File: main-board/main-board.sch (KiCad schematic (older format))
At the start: 69 parts, among them J1 NVIDIA_Jetson_NX_Dev_40pin_Co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, J10 FSESC_6.6_COMM_Minimal, J11 FSESC_6.6_COMM_Minimal, J12 FSESC_6.6_COMM_Minimal, J13 FSESC_6.6_COMM_Minimal, J14 ArducamPTZ, J2 NVIDIA_Jetson_NX_Dev_Button_C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, J3 Conn_01x02, J4 Conn_01x02, J5 Conn_01x02, J6 FSESC_6.6_COMM_Minimal, J7 QWIIC_Generic_Conn, J8 Conn_01x03, J9 FSESC_6.6_COMM_Minimal, M1 Fan_3pin, M2 Fan_3pin, M3 Fan_3pin, Q1 Q_NMOS_GSD, Q2 Q_NMOS_GSD, Q4 Q_NMOS_GSD, Q5 Q_NMOS_GSD, Q6 Q_NMOS_GSD, Q7 Q_NMOS_GSD, Q8 Q_NMOS_GSD, U1 RFM95W_Adafruit_Breakout, U10 Analog Temp Sensor, U11 Adafruit_GPS_V3, U12 SN74AHCT125D, U2 TDK_I3A4W008A033V, U3 TDK_I3A4W008A033V, U5 Teensy_4.1, U6 Analog Temp Sensor, U7 Analog Temp Sensor, U8 Analog Temp Sensor, U9 Analog Temp Sensor

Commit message: Shooouuulld be fully routed
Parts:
- added J15: Angle Sensor, Connector_JST:JST_PH_B6B-PH-K_1x06_P2.00mm_Vertical, symbol Connector_Generic:Conn_01x06
- added SYM1: SYM_Magnet_Small, symbol Graphic:SYM_Magnet_Small
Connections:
- net +3V3: now also J15.1 (Pin_1)
- net ADC3: now also U5.45 (P38); no longer U5.33 (P26)
- net ADC5: now also U5.33 (P26); no longer U5.48 (P41)
- net ADC_12V: now also U5.47 (P40); no longer U5.46 (P39)
- net ADC_5V: now also U5.46 (P39); no longer U5.45 (P38)
- net ADC_BATT: now also U5.48 (P41); no longer U5.47 (P40)
- net GND: now also J15.2 (Pin_2)
- net M1_RX: now also U5.41 (P34); no longer U5.2 (P0)
- net M1_TX: now also U5.42 (P35); no longer U5.3 (P1)
- net M2_RX: now also U5.35 (P28); no longer U5.9 (P7)
- net M2_TX: now also U5.36 (P29); no longer U5.10 (P8)
- net M4_RX: now also U5.9 (P7); no longer U5.25 (P21)
- net M4_TX: now also U5.10 (P8); no longer U5.24 (P20)
- net M5_RX: now also U5.25 (P21); no longer U5.35 (P28)
- net M5_TX: now also U5.24 (P20); no longer U5.36 (P29)
- net M6_RX: now also U5.2 (P0); no longer U5.41 (P34)
- net M6_TX: now also U5.3 (P1); no longer U5.42 (P35)
- net MISO: now also J15.4 (Pin_4)
- net MOSI: now also J15.3 (Pin_3)
- net SCK: now also J15.5 (Pin_5)
- net Angle_CS: now reaches U5.11 (P9)
- net Angle_CS: now also J15.6 (Pin_6)
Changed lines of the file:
@@
 Text Label 7500 5500 0    50   ~ 0
 ADC2
-Text Label 6600 6500 2    50   ~ 0
+Text Label 7500 6600 0    50   ~ 0
 ADC3
 Text Label 6600 6600 2    50   ~ 0
 ADC4
-Text Label 7500 6300 0    50   ~ 0
+Text Label 6600 6500 2    50   ~ 0
 ADC5
 $Comp
@@
 	8300 9950 8100 9950
 Connection ~ 8750 10150
-Text Label 6600 4900 2    50   ~ 0
+Text Label 7500 7000 0    50   ~ 0
 M1_RX
-Text Label 6600 5000 2    50   ~ 0
+Text Label 7500 6900 0    50   ~ 0
 M1_TX
-Text Label 6600 5600 2    50   ~ 0
+Text Label 6600 6700 2    50   ~ 0
 M2_RX
-Text Label 6600 5700 2    50   ~ 0
+Text Label 6600 6800 2    50   ~ 0
 M2_TX
 Text Label 7500 6000 0    50   ~ 0
@@
 Text Label 7500 5900 0    50   ~ 0
 M3_RX
-Text Label 6600 6700 2    50   ~ 0
+Text Label 7500 5300 0    50   ~ 0
 M5_RX
-Text Label 6600 6800 2    50   ~ 0
+Text Label 7500 5400 0    50   ~ 0
 M5_TX
-Text Label 7500 5400 0    50   ~ 0
+Text Label 6600 5700 2    50   ~ 0
 M4_TX
-Text Label 7500 5300 0    50   ~ 0
+Text Label 6600 5600 2    50   ~ 0
 M4_RX
-Text Label 7500 7000 0    50   ~ 0
+Text Label 6600 4900 2    50   ~ 0
 M6_RX
-Text Label 7500 6900 0    50   ~ 0
-M6_TX
 Text Label 6600 5100 2    50   ~ 0
 ARGB_Data
@@
 Text Label 7500 6700 0    50   ~ 0
 Fan3_Control
-Text Label 7500 6600 0    50   ~ 0
+Text Label 7500 6500 0    50   ~ 0
 ADC_5V
-Text Label 7500 6400 0    50   ~ 0
+Text Label 7500 6300 0    50   ~ 0
 ADC_BATT
 Text Label 8050 3250 0    50   ~ 0
@@
 Text Label 6300 3250 0    50   ~ 0
 ADC_12V
-Text Label 7500 6500 0    50   ~ 0
+Text Label 7500 6400 0    50   ~ 0
 ADC_12V
 $Comp
@@
 	1    0    0    -1
 $EndComp
+$Comp
+L Connector_Generic:Conn_01x06 J15
+U 1 1 6134C702
+P 14050 8800
+F 0 "J15" H 14130 8792 50  0000 L CNN
+F 1 "Angle Sensor" H 14130 8701 50  0000 L CNN
+F 2 "Connector_JST:JST_PH_B6B-PH-K_1x06_P2.00mm_Vertical" H 14050 8800 50  0001 C CNN
+F 3 "AS5047D-ATSTCT-ND" H 14050 8800 50  0001 C CNN
+	1    14050 8800
+	1    0    0    -1
+$EndComp
+$Comp
+L Graphic:SYM_Magnet_Small SYM1
+U 1 1 6134F49B
+P 15000 8850
+F 0 "SYM1" H 15000 8990 50  0001 C CNN
+F 1 "SYM_Magnet_Small" H 15000 8725 50  0001 C CNN
+F 2 "" H 15000 8675 50  0001 C CNN
+F 3 "~" H 15030 8650 50  0001 C CNN
+F 4 "469-1025-ND" H 15000 8850 50  0001 C CNN "Digikey Part Num"
+	1    15000 8850
+	1    0    0    -1
+$EndComp
+$Comp
+L power:+3.3V #PWR0103
+U 1 1 61354FD1
+P 13500 8600
+F 0 "#PWR0103" H 13500 8450 50  0001 C CNN
+F 1 "+3.3V" H 13515 8773 50  0000 C CNN
+F 2 "" H 13500 8600 50  0001 C CNN
+F 3 "" H 13500 8600 50  0001 C CNN
+	1    13500 8600
+	1    0    0    -1
+$EndComp
+$Comp
+L power:GND #PWR0104
+U 1 1 613553D9
+P 13350 8700
+F 0 "#PWR0104" H 13350 8450 50  0001 C CNN
+F 1 "GND" H 13355 8527 50  0000 C CNN
+F 2 "" H 13350 8700 50  0001 C CNN
+F 3 "" H 13350 8700 50  0001 C CNN
+	1    13350 8700
+	1    0    0    -1
+$EndComp
+Wire Wire Line
+	13850 8600 13500 8600
+Wire Wire Line
+	13350 8700 13850 8700
+Text Label 13850 8800 2    50   ~ 0
+MOSI
+Text Label 13850 8900 2    50   ~ 0
+MISO
+Text Label 13850 9000 2    50   ~ 0
+SCK
+Text Label 13850 9100 2    50   ~ 0
+Angle_CS
+Text Label 6600 5800 2    50   ~ 0
+Angle_CS
+Text Label 6600 5000 2    50   ~ 0
+M6_TX
 $EndSCHEMATC

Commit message: XT60 Fix
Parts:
- removed BT1: Battery, Connector_AMASS:AMASS_XT60-M_1x02_P7.20mm_Vertical, symbol Device:Battery
- added BT1: XT60_Battery_Connector, Connector_AMASS:AMASS_XT60-M_1x02_P7.20mm_Vertical, symbol ASTRA_Library:XT60_Battery_Connector
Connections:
- net +BATT: now also BT1.2 (Pos)
- net GND: now also BT1.1 (Neg)
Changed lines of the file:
@@
-	1    0    0    -1
-$EndComp
-$Comp
-L Device:Battery BT?
-U 1 1 60FDACF1
-P 3750 1900
-AR Path="/60751D8F/60FDACF1" Ref="BT?"  Part="1"
-AR Path="/60FDACF1" Ref="BT1"  Part="1"
-F 0 "BT1" H 3858 1946 50  0000 L CNN
-F 1 "Battery" H 3858 1855 50  0000 L CNN
-F 2 "Connector_AMASS:AMASS_XT60-M_1x02_P7.20mm_Vertical" V 3750 1960 50  0001 C CNN
-F 3 "~" V 3750 1960 50  0001 C CNN
-F 4 "~" H 3750 1900 50  0001 C CNN "Digikey Part Num"
-	1    3750 1900
 	1    0    0    -1
 $EndComp
@@
 L power:+BATT #PWR015
 U 1 1 60FDF0DD
-P 3750 1700
-F 0 "#PWR015" H 3750 1550 50  0001 C CNN
-F 1 "+BATT" H 3765 1873 50  0000 C CNN
-F 2 "" H 3750 1700 50  0001 C CNN
-F 3 "" H 3750 1700 50  0001 C CNN
-	1    3750 1700
+P 3700 1650
+F 0 "#PWR015" H 3700 1500 50  0001 C CNN
+F 1 "+BATT" H 3715 1823 50  0000 C CNN
+F 2 "" H 3700 1650 50  0001 C CNN
+F 3 "" H 3700 1650 50  0001 C CNN
+	1    3700 1650
 	1    0    0    -1
 $EndComp
@@
 L power:GND #PWR016
 U 1 1 60FDF640
-P 3750 2100
-F 0 "#PWR016" H 3750 1850 50  0001 C CNN
-F 1 "GND" H 3755 1927 50  0000 C CNN
-F 2 "" H 3750 2100 50  0001 C CNN
-F 3 "" H 3750 2100 50  0001 C CNN
-	1    3750 2100
+P 3700 2150
+F 0 "#PWR016" H 3700 1900 50  0001 C CNN
+F 1 "GND" H 3705 1977 50  0000 C CNN
+F 2 "" H 3700 2150 50  0001 C CNN
+F 3 "" H 3700 2150 50  0001 C CNN
+	1    3700 2150
 	1    0    0    -1
 $EndComp
@@
 Text Label 6600 5000 2    50   ~ 0
 M6_TX
+$Comp
+L ASTRA_Library:XT60_Battery_Connector BT1
+U 1 1 614D559C
+P 3700 1900
+F 0 "BT1" H 3572 1946 50  0000 R CNN
+F 1 "XT60_Battery_Connector" H 3572 1855 50  0000 R CNN
+F 2 "Connector_AMASS:AMASS_XT60-M_1x02_P7.20mm_Vertical" H 3700 1900 50  0001 C CNN
+F 3 "" H 3700 1900 50  0001 C CNN
+	1    3700 1900
+	1    0    0    -1
+$EndComp
 $EndSCHEMATC

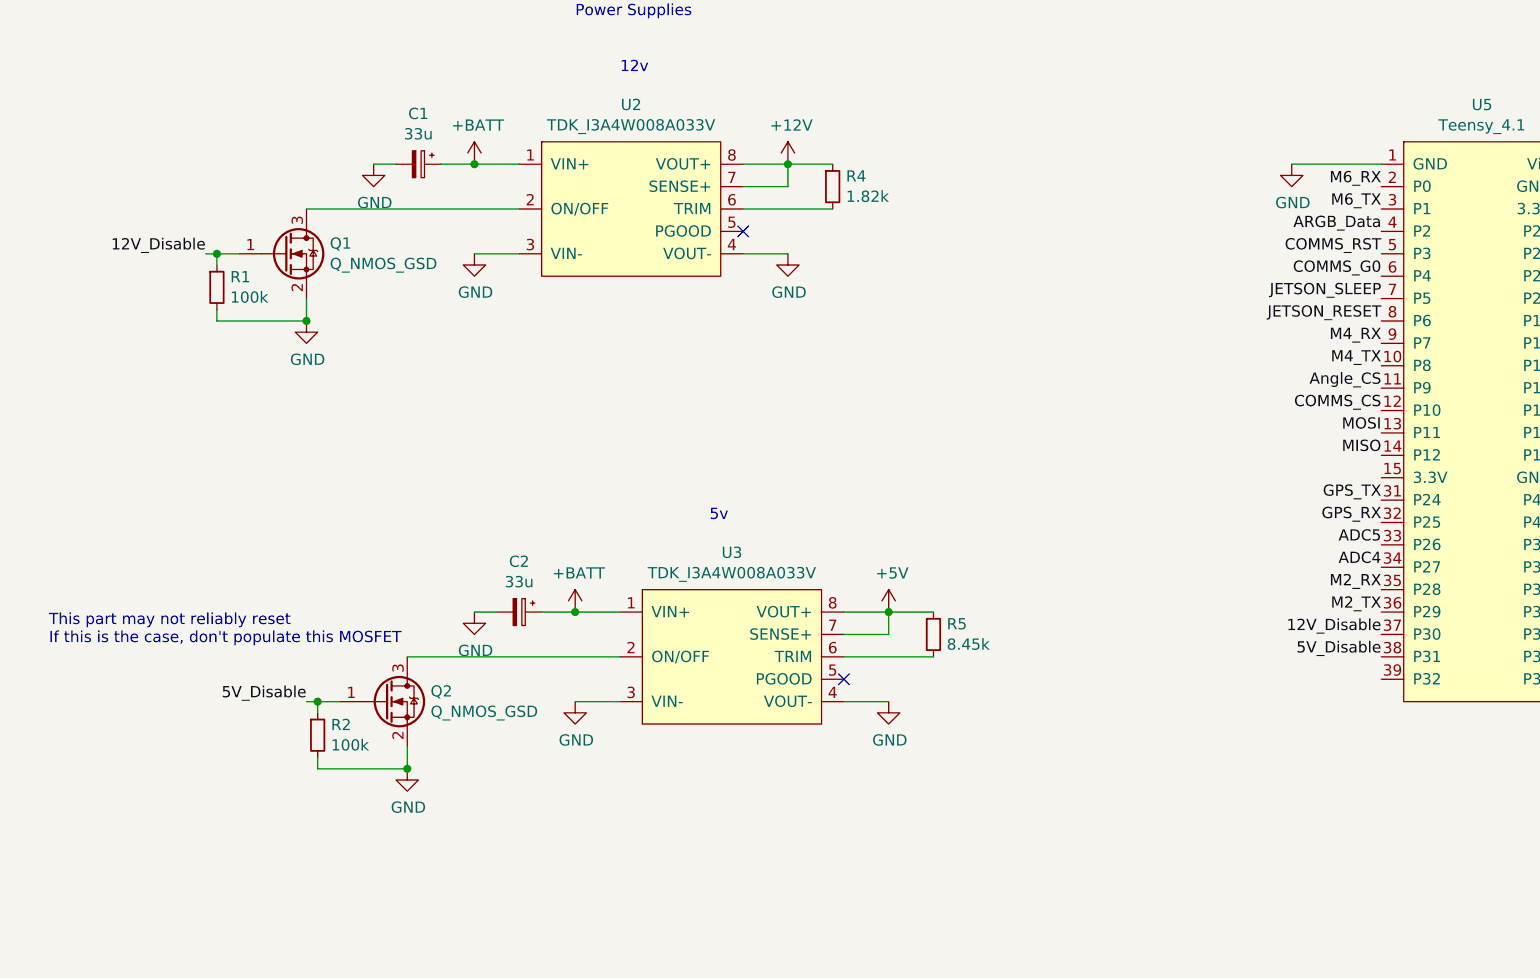
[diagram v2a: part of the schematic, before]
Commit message: Implemented post SAR fixes
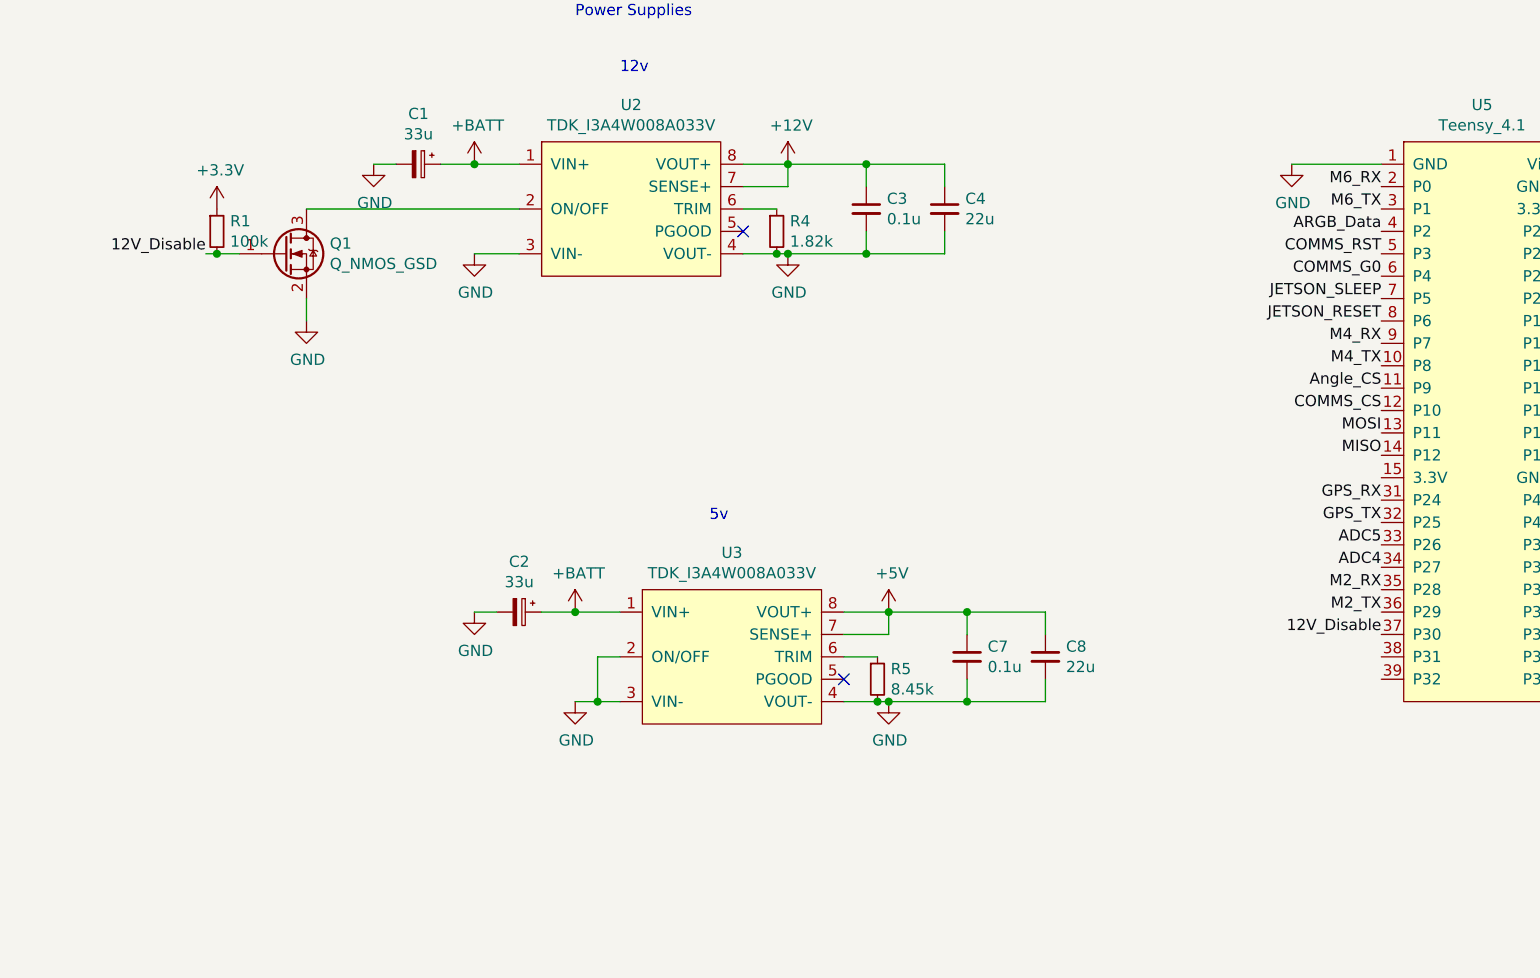
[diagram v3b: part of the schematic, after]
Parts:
- removed Q2: Q_NMOS_GSD, Package_TO_SOT_SMD:SOT-23, symbol Device:Q_NMOS_GSD
- removed R2: 100k, Resistor_SMD:R_0603_1608Metric, symbol Device:R_Small
- added C3, C7: 0.1u, Capacitor_SMD:C_0603_1608Metric, symbol Device:C_Small
- added C4, C8: 22u, Capacitor_SMD:C_1210_3225Metric, symbol Device:C_Small
- H1, H2, H3, H4: footprint MountingHole:MountingHole_3.2mm_M3 -> MountingHole:MountingHole_3.2mm_M3_Pad
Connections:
- net +12V: now also C3.1, C4.1; no longer R4.1
- net +3V3: now also R1.1
- net +5V: now also C7.1, C8.1; no longer R5.1
- net 12V_Disable: now also R1.2; no longer R1.1
- net GND: now also R4.2, R5.2, U3.2 (ON/OFF), C3.2, C4.2, C7.2, C8.2; no longer R1.2
- net GPS_RX: now also U5.31 (P24); no longer U5.32 (P25)
- net GPS_TX: now also U5.32 (P25); no longer U5.31 (P24)
- net at U2.6 (TRIM): now also R4.1; no longer R4.2
- net at U3.6 (TRIM): now also R5.1; no longer R5.2
- net 5V_Disable: no longer names the net of U5.38 (P31)
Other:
- note removed: "This part may not reliably reset\nIf this is the case, don't populate this MOSFET"
- moved on the sheet: R1, R4, R5
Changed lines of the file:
@@
 Wire Wire Line
 	15950 5000 15700 5000
+Text Label 6600 6300 2    50   ~ 0
+GPS_RX
 Text Label 6600 6400 2    50   ~ 0
-GPS_RX
-Text Label 6600 6300 2    50   ~ 0
 GPS_TX
 Text Label 6600 5900 2    50   ~ 0
@@
 $EndComp
 Wire Wire Line
-	3950 5200 3750 5200
+	3950 5200 3900 5200
 $Comp
 L power:+12V #PWR017
@@
 L Device:R_Small R1
 U 1 1 61269DDD
-P 1400 5350
-F 0 "R1" H 1459 5396 50  0000 L CNN
-F 1 "100k" H 1459 5305 50  0000 L CNN
-F 2 "Resistor_SMD:R_0603_1608Metric" H 1400 5350 50  0001 C CNN
-F 3 "~" H 1400 5350 50  0001 C CNN
-F 4 "311-100KHRCT-ND" H 1400 5350 50  0001 C CNN "Digikey Part Num"
-	1    1400 5350
-	1    0    0    -1
-$EndComp
-Wire Wire Line
-	1800 5500 1400 5500
-Wire Wire Line
-	1400 5500 1400 5450
-Connection ~ 1800 5500
-Wire Wire Line
-	1400 5250 1400 5200
+P 1400 5100
+F 0 "R1" H 1459 5146 50  0000 L CNN
+F 1 "100k" H 1459 5055 50  0000 L CNN
+F 2 "Resistor_SMD:R_0603_1608Metric" H 1400 5100 50  0001 C CNN
+F 3 "~" H 1400 5100 50  0001 C CNN
+F 4 "311-100KHRCT-ND" H 1400 5100 50  0001 C CNN "Digikey Part Num"
+	1    1400 5100
+	1    0    0    -1
+$EndComp
 Connection ~ 1400 5200
 Wire Wire Line
@@
 L Device:R_Small R4
 U 1 1 6127ADA1
-P 4150 4900
-F 0 "R4" H 4209 4946 50  0000 L CNN
-F 1 "1.82k" H 4209 4855 50  0000 L CNN
-F 2 "Resistor_SMD:R_0603_1608Metric" H 4150 4900 50  0001 C CNN
-F 3 "~" H 4150 4900 50  0001 C CNN
-F 4 "311-1.82KHRCT-ND" H 4150 4900 50  0001 C CNN "Digikey Part Num"
-	1    4150 4900
-	1    0    0    -1
-$EndComp
-Wire Wire Line
-	4150 4800 3950 4800
-Wire Wire Line
-	4150 5000 3750 5000
+P 3900 5100
+F 0 "R4" H 3959 5146 50  0000 L CNN
+F 1 "1.82k" H 3959 5055 50  0000 L CNN
+F 2 "Resistor_SMD:R_0603_1608Metric" H 3900 5100 50  0001 C CNN
+F 3 "~" H 3900 5100 50  0001 C CNN
+F 4 "311-1.82KHRCT-ND" H 3900 5100 50  0001 C CNN "Digikey Part Num"
+	1    3900 5100
+	1    0    0    -1
+$EndComp
 $Comp
 L Device:CP_Small C1
@@
 $EndComp
 Wire Wire Line
-	3200 7200 3000 7200
+	3200 7200 3100 7200
 $Comp
 L power:GND #PWR021
@@
 $EndComp
 Wire Wire Line
-	4400 7200 4200 7200
+	4400 7200 4350 7200
 Wire Wire Line
 	4400 6800 4200 6800
@@
 Connection ~ 4400 6800
 $Comp
-L Device:Q_NMOS_GSD Q2
-U 1 1 612A9D07
-P 2150 7200
-F 0 "Q2" H 2354 7246 50  0000 L CNN
-F 1 "Q_NMOS_GSD" H 2354 7155 50  0000 L CNN
-F 2 "Package_TO_SOT_SMD:SOT-23" H 2350 7300 50  0001 C CNN
-F 3 "~" H 2150 7200 50  0001 C CNN
-F 4 "SSM3K2615RLFCT-ND" H 2150 7200 50  0001 C CNN "Digikey Part Num"
-	1    2150 7200
-	1    0    0    -1
-$EndComp
-Wire Wire Line
-	3200 7000 2250 7000
-$Comp
-L power:GND #PWR05
-U 1 1 612A9D12
-P 2250 7500
-F 0 "#PWR05" H 2250 7250 50  0001 C CNN
-F 1 "GND" H 2255 7327 50  0000 C CNN
-F 2 "" H 2250 7500 50  0001 C CNN
-F 3 "" H 2250 7500 50  0001 C CNN
-	1    2250 7500
-	1    0    0    -1
-$EndComp
-Wire Wire Line
-	2250 7500 2250 7400
-Text Label 1800 7200 2    50   ~ 0
-5V_Disable
-Wire Wire Line
-	1800 7200 1850 7200
-$Comp
-L Device:R_Small R2
-U 1 1 612A9D1F
-P 1850 7350
-F 0 "R2" H 1909 7396 50  0000 L CNN
-F 1 "100k" H 1909 7305 50  0000 L CNN
-F 2 "Resistor_SMD:R_0603_1608Metric" H 1850 7350 50  0001 C CNN
-F 3 "~" H 1850 7350 50  0001 C CNN
-F 4 "311-100KHRCT-ND" H 1850 7350 50  0001 C CNN "Digikey Part Num"
-	1    1850 7350
-	1    0    0    -1
-$EndComp
-Wire Wire Line
-	2250 7500 1850 7500
-Wire Wire Line
-	1850 7500 1850 7450
-Connection ~ 2250 7500
-Wire Wire Line
-	1850 7250 1850 7200
-Connection ~ 1850 7200
-Wire Wire Line
-	1850 7200 1950 7200
-$Comp
 L Device:R_Small R5
 U 1 1 612A9D2F
-P 4600 6900
-F 0 "R5" H 4659 6946 50  0000 L CNN
-F 1 "8.45k" H 4659 6855 50  0000 L CNN
-F 2 "Resistor_SMD:R_0603_1608Metric" H 4600 6900 50  0001 C CNN
-F 3 "~" H 4600 6900 50  0001 C CNN
-F 4 "311-8.45KHRCT-ND" H 4600 6900 50  0001 C CNN "Digikey Part Num"
-	1    4600 6900
-	1    0    0    -1
-$EndComp
-Wire Wire Line
-	4600 6800 4400 6800
-Wire Wire Line
-	4600 7000 4200 7000
+P 4350 7100
+F 0 "R5" H 4409 7146 50  0000 L CNN
+F 1 "8.45k" H 4409 7055 50  0000 L CNN
+F 2 "Resistor_SMD:R_0603_1608Metric" H 4350 7100 50  0001 C CNN
+F 3 "~" H 4350 7100 50  0001 C CNN
+F 4 "311-8.45KHRCT-ND" H 4350 7100 50  0001 C CNN "Digikey Part Num"
+	1    4350 7100
+	1    0    0    -1
+$EndComp
 $Comp
 L Device:CP_Small C2
@@
 Wire Wire Line
 	2650 6800 2550 6800
-Text Label 6600 7000 2    50   ~ 0
-5V_Disable
 $Comp
 L power:+3.3V #PWR044
@@
 Wire Wire Line
 	8350 5000 7500 5000
-Text Notes 650  6950 0    50   ~ 0
-This part may not reliably reset\nIf this is the case, don't populate this MOSFET
 Text Label 6300 3250 0    50   ~ 0
 ADC_12V
@@
 F 0 "H1" H 1050 8846 50  0000 L CNN
 F 1 "MountingHole" H 1050 8755 50  0000 L CNN
-F 2 "MountingHole:MountingHole_3.2mm_M3" H 950 8800 50  0001 C CNN
+F 2 "MountingHole:MountingHole_3.2mm_M3_Pad" H 950 8800 50  0001 C CNN
 F 3 "~" H 950 8800 50  0001 C CNN
 	1    950  8800
@@
 F 0 "H2" H 1050 9046 50  0000 L CNN
 F 1 "MountingHole" H 1050 8955 50  0000 L CNN
-F 2 "MountingHole:MountingHole_3.2mm_M3" H 950 9000 50  0001 C CNN
+F 2 "MountingHole:MountingHole_3.2mm_M3_Pad" H 950 9000 50  0001 C CNN
 F 3 "~" H 950 9000 50  0001 C CNN
 	1    950  9000
@@
 F 0 "H3" H 1050 9246 50  0000 L CNN
 F 1 "MountingHole" H 1050 9155 50  0000 L CNN
-F 2 "MountingHole:MountingHole_3.2mm_M3" H 950 9200 50  0001 C CNN
+F 2 "MountingHole:MountingHole_3.2mm_M3_Pad" H 950 9200 50  0001 C CNN
 F 3 "~" H 950 9200 50  0001 C CNN
 	1    950  9200
@@
 F 0 "H4" H 1050 9446 50  0000 L CNN
 F 1 "MountingHole" H 1050 9355 50  0000 L CNN
-F 2 "MountingHole:MountingHole_3.2mm_M3" H 950 9400 50  0001 C CNN
+F 2 "MountingHole:MountingHole_3.2mm_M3_Pad" H 950 9400 50  0001 C CNN
 F 3 "~" H 950 9400 50  0001 C CNN
 	1    950  9400
@@
 	1    0    0    -1
 $EndComp
+Wire Wire Line
+	3900 5000 3750 5000
+Connection ~ 3900 5200
+Wire Wire Line
+	3900 5200 3750 5200
+Wire Wire Line
+	4350 7000 4200 7000
+Connection ~ 4350 7200
+Wire Wire Line
+	4350 7200 4200 7200
+$Comp
+L Device:C_Small C3
+U 1 1 62452E85
+P 4300 5000
+F 0 "C3" H 4392 5046 50  0000 L CNN
+F 1 "0.1u" H 4392 4955 50  0000 L CNN
+F 2 "Capacitor_SMD:C_0603_1608Metric" H 4300 5000 50  0001 C CNN
+F 3 "~" H 4300 5000 50  0001 C CNN
+	1    4300 5000
+	1    0    0    -1
+$EndComp
+Wire Wire Line
+	3950 4800 4300 4800
+Wire Wire Line
+	4650 4800 4650 4900
+Wire Wire Line
+	4300 4900 4300 4800
+Connection ~ 4300 4800
+Wire Wire Line
+	4300 4800 4650 4800
+Wire Wire Line
+	3950 5200 4300 5200
+Wire Wire Line
+	4650 5200 4650 5100
+Connection ~ 3950 5200
+Wire Wire Line
+	4300 5100 4300 5200
+Connection ~ 4300 5200
+Wire Wire Line
+	4300 5200 4650 5200
+Wire Wire Line
+	3200 7000 3100 7000
+Wire Wire Line
+	3100 7000 3100 7200
+Connection ~ 3100 7200
+Wire Wire Line
+	3100 7200 3000 7200
+$Comp
+L Device:C_Small C7
+U 1 1 624BC7F6
+P 4750 7000
+F 0 "C7" H 4842 7046 50  0000 L CNN
+F 1 "0.1u" H 4842 6955 50  0000 L CNN
+F 2 "Capacitor_SMD:C_0603_1608Metric" H 4750 7000 50  0001 C CNN
+F 3 "~" H 4750 7000 50  0001 C CNN
+	1    4750 7000
+	1    0    0    -1
+$EndComp
+Wire Wire Line
+	4400 6800 4750 6800
+Wire Wire Line
+	5100 6800 5100 6900
+Wire Wire Line
+	4750 6900 4750 6800
+Connection ~ 4750 6800
+Wire Wire Line
+	4750 6800 5100 6800
+Wire Wire Line
+	4400 7200 4750 7200
+Wire Wire Line
+	5100 7200 5100 7100
+Wire Wire Line
+	4750 7100 4750 7200
+Connection ~ 4750 7200
+Wire Wire Line
+	4750 7200 5100 7200
+Connection ~ 4400 7200
+$Comp
+L power:+3.3V #PWR0105
+U 1 1 624D0C46
+P 1400 5000
+F 0 "#PWR0105" H 1400 4850 50  0001 C CNN
+F 1 "+3.3V" H 1415 5173 50  0000 C CNN
+F 2 "" H 1400 5000 50  0001 C CNN
+F 3 "" H 1400 5000 50  0001 C CNN
+	1    1400 5000
+	1    0    0    -1
+$EndComp
+$Comp
+L Device:C_Small C4
+U 1 1 625377A1
+P 4650 5000
+F 0 "C4" H 4742 5046 50  0000 L CNN
+F 1 "22u" H 4742 4955 50  0000 L CNN
+F 2 "Capacitor_SMD:C_1210_3225Metric" H 4650 5000 50  0001 C CNN
+F 3 "~" H 4650 5000 50  0001 C CNN
+F 4 "311-2053-1-ND" H 4650 5000 50  0001 C CNN "Digikey Part Num"
+	1    4650 5000
+	1    0    0    -1
+$EndComp
+$Comp
+L Device:C_Small C8
+U 1 1 62539002
+P 5100 7000
+F 0 "C8" H 5192 7046 50  0000 L CNN
+F 1 "22u" H 5192 6955 50  0000 L CNN
+F 2 "Capacitor_SMD:C_1210_3225Metric" H 5100 7000 50  0001 C CNN
+F 3 "~" H 5100 7000 50  0001 C CNN
+F 4 "311-2053-1-ND" H 5100 7000 50  0001 C CNN "Digikey Part Num"
+	1    5100 7000
+	1    0    0    -1
+$EndComp
